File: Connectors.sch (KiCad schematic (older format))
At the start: 14 parts, among them J2 Conn_01x08_Male, J3 Conn_01x08_Male, J4 Conn_01x08_Male

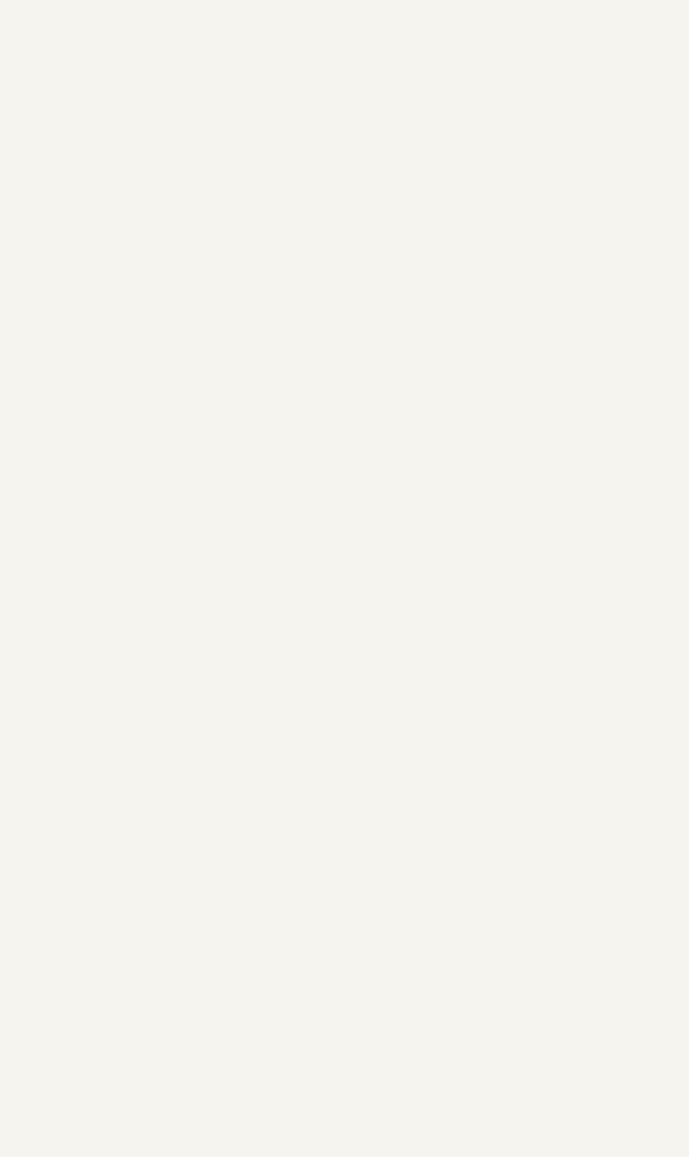
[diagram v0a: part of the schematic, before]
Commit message: start adding usb-c
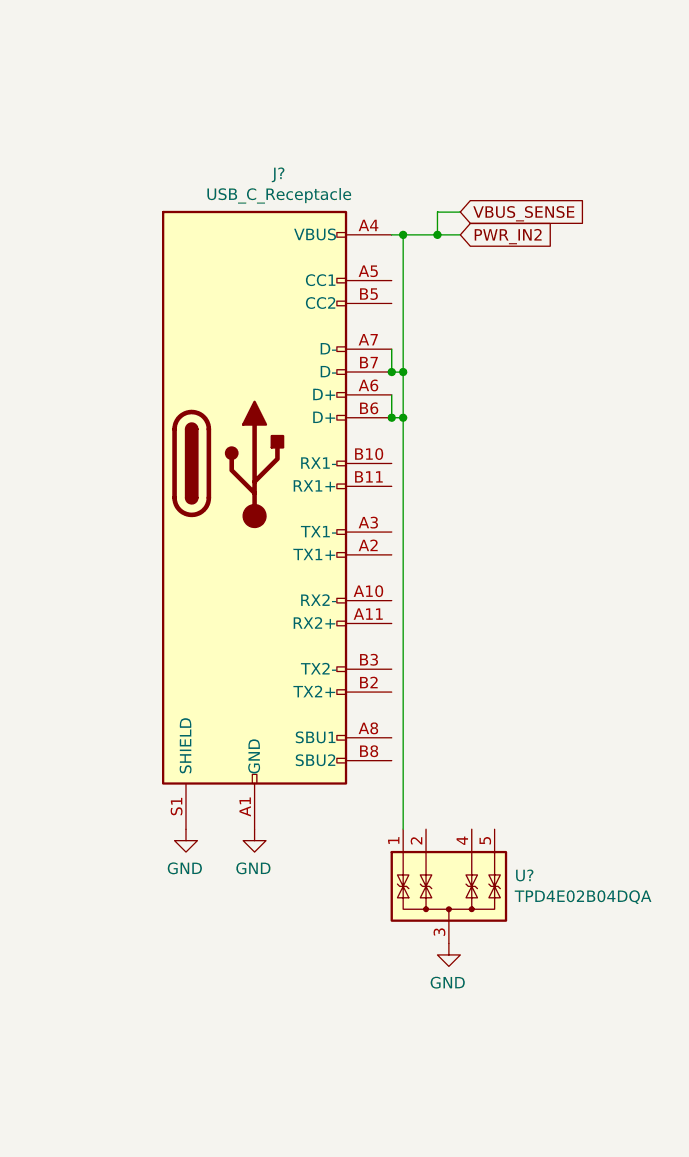
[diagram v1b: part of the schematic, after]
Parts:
- added J?: USB_C_Receptacle, symbol Connector:USB_C_Receptacle
- added U?: TPD4E02B04DQA, Package_SON:USON-10_2.5x1.0mm_P0.5mm, symbol Power_Protection:TPD4E02B04DQA
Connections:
- net GND: now also J?.A1 (GND), J?.A12 (GND), J?.B1 (GND), J?.B12 (GND), J?.S1 (SHIELD), U?.3 (G), U?.8 (G)
- new net PWR_IN2: J?.A4 (VBUS), J?.A6 (D+), J?.A7 (D-), J?.A9 (VBUS), J?.B4 (VBUS), J?.B6 (D+), J?.B7 (D-), J?.B9 (VBUS), U?.1 (IO1)
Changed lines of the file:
@@
 EndData
 $EndBitmap
+$Comp
+L Connector:USB_C_Receptacle J?
+U 1 1 61CDAA86
+P 11850 2450
+F 0 "J?" H 11957 3717 50  0000 C CNN
+F 1 "USB_C_Receptacle" H 11957 3626 50  0000 C CNN
+F 2 "" H 12000 2450 50  0001 C CNN
+F 3 "https://www.usb.org/sites/default/files/documents/usb_type-c.zip" H 12000 2450 50  0001 C CNN
+	1    11850 2450
+	1    0    0    -1
+$EndComp
+Text GLabel 12750 1350 2    50   Input ~ 0
+VBUS_SENSE
+$Comp
+L Power_Protection:TPD4E02B04DQA U?
+U 1 1 61CDF2A4
+P 12700 4350
+F 0 "U?" H 12988 4446 50  0000 L CNN
+F 1 "TPD4E02B04DQA" H 12988 4355 50  0000 L CNN
+F 2 "Package_SON:USON-10_2.5x1.0mm_P0.5mm" H 13000 4350 50  0001 L CNN
+F 3 "http://www.ti.com/lit/ds/symlink/tpd4e02b04.pdf" H 12825 4675 50  0001 C CNN
+	1    12700 4350
+	1    0    0    -1
+$EndComp
+$Comp
+L power:GND #PWR?
+U 1 1 61CE1733
+P 12700 4550
+AR Path="/61C29261/61CE1733" Ref="#PWR?"  Part="1"
+AR Path="/61E12439/61CE1733" Ref="#PWR?"  Part="1"
+F 0 "#PWR?" H 12700 4300 50  0001 C CNN
+F 1 "GND" H 12705 4377 50  0000 C CNN
+F 2 "" H 12700 4550 50  0001 C CNN
+F 3 "" H 12700 4550 50  0001 C CNN
+	1    12700 4550
+	-1   0    0    -1
+$EndComp
+$Comp
+L power:GND #PWR?
+U 1 1 61CE227D
+P 11850 4050
+AR Path="/61C29261/61CE227D" Ref="#PWR?"  Part="1"
+AR Path="/61E12439/61CE227D" Ref="#PWR?"  Part="1"
+F 0 "#PWR?" H 11850 3800 50  0001 C CNN
+F 1 "GND" H 11855 3877 50  0000 C CNN
+F 2 "" H 11850 4050 50  0001 C CNN
+F 3 "" H 11850 4050 50  0001 C CNN
+	1    11850 4050
+	-1   0    0    -1
+$EndComp
+$Comp
+L power:GND #PWR?
+U 1 1 61CE293D
+P 11550 4050
+AR Path="/61C29261/61CE293D" Ref="#PWR?"  Part="1"
+AR Path="/61E12439/61CE293D" Ref="#PWR?"  Part="1"
+F 0 "#PWR?" H 11550 3800 50  0001 C CNN
+F 1 "GND" H 11555 3877 50  0000 C CNN
+F 2 "" H 11550 4050 50  0001 C CNN
+F 3 "" H 11550 4050 50  0001 C CNN
+	1    11550 4050
+	-1   0    0    -1
+$EndComp
+Wire Wire Line
+	12450 1450 12500 1450
+Wire Wire Line
+	12500 1450 12500 2050
+Connection ~ 12500 1450
+Wire Wire Line
+	12500 1450 12650 1450
+Wire Wire Line
+	12450 2150 12450 2250
+Wire Wire Line
+	12450 1950 12450 2050
+Wire Wire Line
+	12450 2050 12500 2050
+Connection ~ 12450 2050
+Connection ~ 12500 2050
+Wire Wire Line
+	12500 2050 12500 2250
+Wire Wire Line
+	12450 2250 12500 2250
+Connection ~ 12450 2250
+Connection ~ 12500 2250
+Wire Wire Line
+	12500 2250 12500 4050
+Text GLabel 12750 1450 2    50   Input ~ 0
+PWR_IN2
+Wire Wire Line
+	12750 1350 12650 1350
+Wire Wire Line
+	12650 1350 12650 1450
+Connection ~ 12650 1450
+Wire Wire Line
+	12650 1450 12750 1450
 $EndSCHEMATC

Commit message: working
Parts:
- J6: renamed from J?; footprint (none) -> Connector_USB:USB_C_Receptacle_XKB_U262-16XN-4BVC11
- gave numbers to parts that had none: 1
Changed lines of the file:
@@
 Wire Wire Line
 	3700 3100 3700 3200
-Text GLabel 4500 2500 2    50   Input ~ 0
-STM_CH1
 Wire Wire Line
 	4500 2500 4400 2500
@@
 $EndBitmap
 $Comp
-L Connector:USB_C_Receptacle J?
+L Connector:USB_C_Receptacle J6
 U 1 1 61CDAA86
 P 11850 2450
-F 0 "J?" H 11957 3717 50  0000 C CNN
+F 0 "J6" H 11957 3717 50  0000 C CNN
 F 1 "USB_C_Receptacle" H 11957 3626 50  0000 C CNN
-F 2 "" H 12000 2450 50  0001 C CNN
+F 2 "Connector_USB:USB_C_Receptacle_XKB_U262-16XN-4BVC11" H 12000 2450 50  0001 C CNN
 F 3 "https://www.usb.org/sites/default/files/documents/usb_type-c.zip" H 12000 2450 50  0001 C CNN
 	1    11850 2450
@@
 VBUS_SENSE
 $Comp
-L Power_Protection:TPD4E02B04DQA U?
+L Power_Protection:TPD4E02B04DQA U15
 U 1 1 61CDF2A4
 P 12700 4350
-F 0 "U?" H 12988 4446 50  0000 L CNN
+F 0 "U15" H 12988 4446 50  0000 L CNN
 F 1 "TPD4E02B04DQA" H 12988 4355 50  0000 L CNN
 F 2 "Package_SON:USON-10_2.5x1.0mm_P0.5mm" H 13000 4350 50  0001 L CNN
@@
 $EndComp
 $Comp
-L power:GND #PWR?
+L power:GND #PWR0153
 U 1 1 61CE1733
 P 12700 4550
-AR Path="/61C29261/61CE1733" Ref="#PWR?"  Part="1"
+AR Path="/61C29261/61CE1733" Ref="#PWR0153"  Part="1"
 AR Path="/61E12439/61CE1733" Ref="#PWR?"  Part="1"
-F 0 "#PWR?" H 12700 4300 50  0001 C CNN
+F 0 "#PWR0153" H 12700 4300 50  0001 C CNN
 F 1 "GND" H 12705 4377 50  0000 C CNN
 F 2 "" H 12700 4550 50  0001 C CNN
@@
 $EndComp
 $Comp
-L power:GND #PWR?
+L power:GND #PWR0154
 U 1 1 61CE227D
 P 11850 4050
-AR Path="/61C29261/61CE227D" Ref="#PWR?"  Part="1"
+AR Path="/61C29261/61CE227D" Ref="#PWR0154"  Part="1"
 AR Path="/61E12439/61CE227D" Ref="#PWR?"  Part="1"
-F 0 "#PWR?" H 11850 3800 50  0001 C CNN
+F 0 "#PWR0154" H 11850 3800 50  0001 C CNN
 F 1 "GND" H 11855 3877 50  0000 C CNN
 F 2 "" H 11850 4050 50  0001 C CNN
@@
 $EndComp
 $Comp
-L power:GND #PWR?
+L power:GND #PWR0155
 U 1 1 61CE293D
 P 11550 4050
-AR Path="/61C29261/61CE293D" Ref="#PWR?"  Part="1"
+AR Path="/61C29261/61CE293D" Ref="#PWR0155"  Part="1"
 AR Path="/61E12439/61CE293D" Ref="#PWR?"  Part="1"
-F 0 "#PWR?" H 11550 3800 50  0001 C CNN
+F 0 "#PWR0155" H 11550 3800 50  0001 C CNN
 F 1 "GND" H 11555 3877 50  0000 C CNN
 F 2 "" H 11550 4050 50  0001 C CNN
@@
 Wire Wire Line
 	12650 1450 12750 1450
+Text GLabel 4500 2500 2    50   Input ~ 0
+STM_CH1
 $EndSCHEMATC

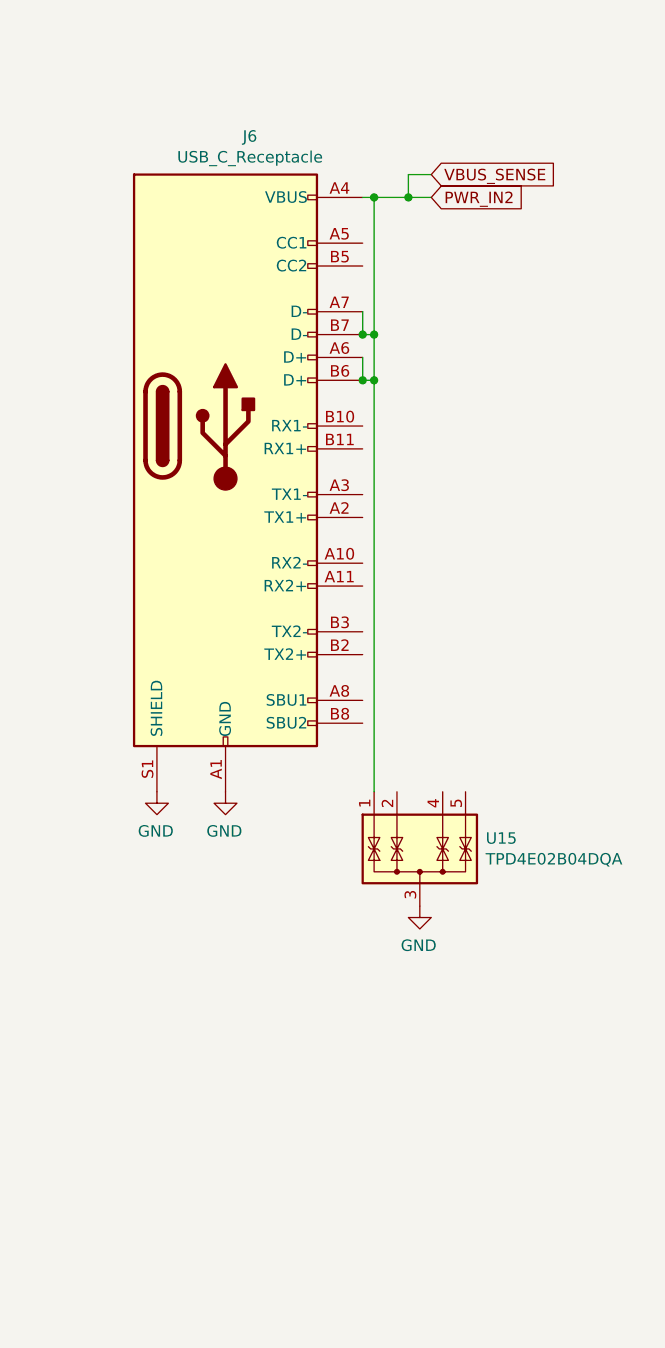
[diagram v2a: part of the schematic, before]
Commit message: start migrating to kicad v6
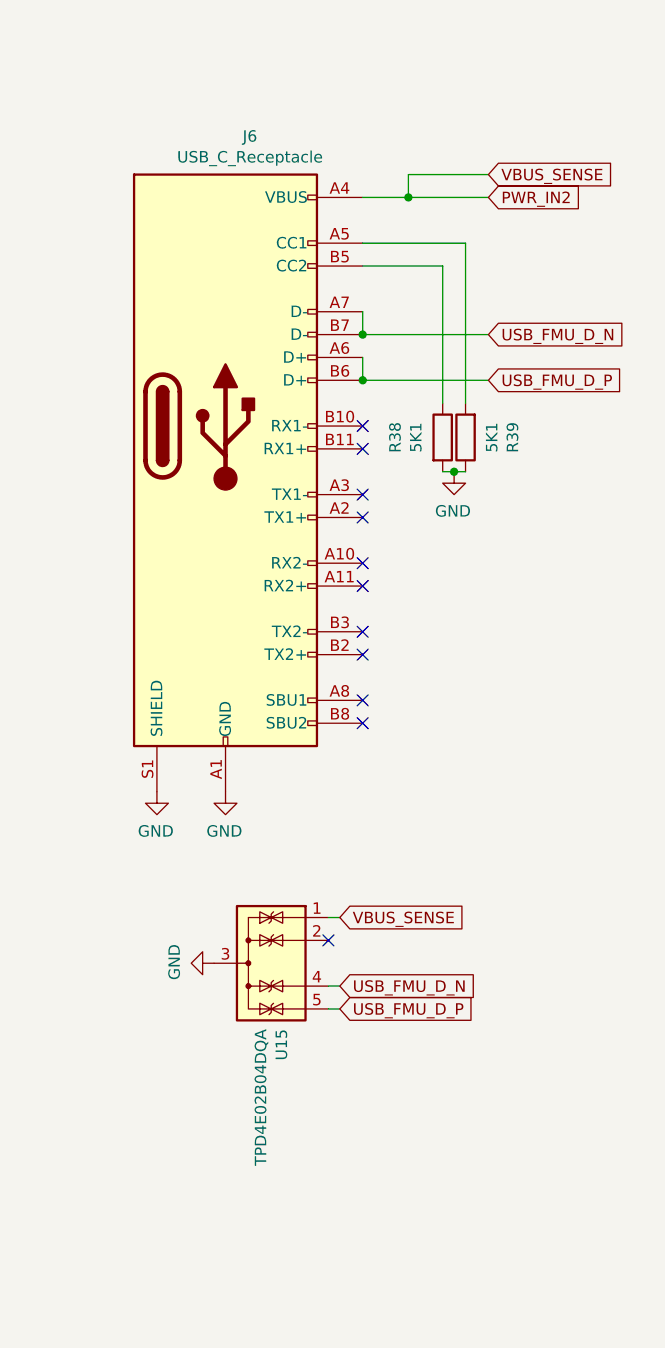
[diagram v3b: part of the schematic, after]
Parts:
- added R38, R39: 5K1, Resistor_SMD:R_0402_1005Metric, symbol Device:R
- J6: Datasheet (none) -> https://www.usb.org/sites/default/files/documents/usb_type-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; Footprint (none) -> Connector_USB:USB_C_Receptacle_XKB_U262-16XN-4BVC11; Manufacturer_Part_Number (none) -> U262-161N-4BVC11; Reference (none) -> J6; Value (none) -> USB_C_Receptacle
- U15: Datasheet (none) -> http://www.ti.com/lit/ds/symlink/tpd4e02b04.pdf; Footprint (none) -> Package_SON:USON-10_2.5x1.0mm_P0.5mm; Manufacturer_Part_Number (none) -> TPD4E02B04DQA; Reference (none) -> U15; Value (none) -> TPD4E02B04DQA
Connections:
- net GND: now also R38.2, R39.1
- net PWR_IN2: no longer J6.A6 (D+), J6.A7 (D-), J6.B6 (D+), J6.B7 (D-)
- net at J6.A5 (CC1): now also R39.2
- net at J6.B5 (CC2): now also R38.1
- net USB_FMU_D_N: now reaches U15.4 (IO3)
- net USB_FMU_D_N: now also J6.A7 (D-), J6.B7 (D-)
- net USB_FMU_D_P: now reaches U15.5 (IO4)
- net USB_FMU_D_P: now also J6.A6 (D+), J6.B6 (D+)
- no-connect marks 6 -> 17
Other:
- moved on the sheet: U15
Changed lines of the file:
@@
 EndData
 $EndBitmap
-$Comp
-L Connector:USB_C_Receptacle J6
-U 1 1 61CDAA86
-P 11850 2450
-F 0 "J6" H 11957 3717 50  0000 C CNN
-F 1 "USB_C_Receptacle" H 11957 3626 50  0000 C CNN
-F 2 "Connector_USB:USB_C_Receptacle_XKB_U262-16XN-4BVC11" H 12000 2450 50  0001 C CNN
-F 3 "https://www.usb.org/sites/default/files/documents/usb_type-c.zip" H 12000 2450 50  0001 C CNN
-	1    11850 2450
-	1    0    0    -1
-$EndComp
-Text GLabel 12750 1350 2    50   Input ~ 0
+Text GLabel 13000 1350 2    50   Input ~ 0
 VBUS_SENSE
-$Comp
-L Power_Protection:TPD4E02B04DQA U15
-U 1 1 61CDF2A4
-P 12700 4350
-F 0 "U15" H 12988 4446 50  0000 L CNN
-F 1 "TPD4E02B04DQA" H 12988 4355 50  0000 L CNN
-F 2 "Package_SON:USON-10_2.5x1.0mm_P0.5mm" H 13000 4350 50  0001 L CNN
-F 3 "http://www.ti.com/lit/ds/symlink/tpd4e02b04.pdf" H 12825 4675 50  0001 C CNN
-	1    12700 4350
-	1    0    0    -1
-$EndComp
-$Comp
-L power:GND #PWR0153
-U 1 1 61CE1733
-P 12700 4550
-AR Path="/61C29261/61CE1733" Ref="#PWR0153"  Part="1"
-AR Path="/61E12439/61CE1733" Ref="#PWR?"  Part="1"
-F 0 "#PWR0153" H 12700 4300 50  0001 C CNN
-F 1 "GND" H 12705 4377 50  0000 C CNN
-F 2 "" H 12700 4550 50  0001 C CNN
-F 3 "" H 12700 4550 50  0001 C CNN
-	1    12700 4550
-	-1   0    0    -1
-$EndComp
 $Comp
 L power:GND #PWR0154
@@
 	-1   0    0    -1
 $EndComp
-Wire Wire Line
-	12450 1450 12500 1450
-Wire Wire Line
-	12500 1450 12500 2050
-Connection ~ 12500 1450
-Wire Wire Line
-	12500 1450 12650 1450
-Wire Wire Line
-	12450 2150 12450 2250
-Wire Wire Line
-	12450 1950 12450 2050
-Wire Wire Line
-	12450 2050 12500 2050
-Connection ~ 12450 2050
-Connection ~ 12500 2050
-Wire Wire Line
-	12500 2050 12500 2250
-Wire Wire Line
-	12450 2250 12500 2250
-Connection ~ 12450 2250
-Connection ~ 12500 2250
-Wire Wire Line
-	12500 2250 12500 4050
-Text GLabel 12750 1450 2    50   Input ~ 0
+Text GLabel 13000 1450 2    50   Input ~ 0
 PWR_IN2
 Wire Wire Line
-	12750 1350 12650 1350
+	13000 1350 12650 1350
 Wire Wire Line
 	12650 1350 12650 1450
 Connection ~ 12650 1450
 Wire Wire Line
-	12650 1450 12750 1450
+	12650 1450 13000 1450
 Text GLabel 4500 2500 2    50   Input ~ 0
 STM_CH1
+Wire Wire Line
+	12450 1950 12450 2050
+Wire Wire Line
+	12450 2150 12450 2250
+Text GLabel 13000 2050 2    50   Input ~ 0
+USB_FMU_D_N
+Text GLabel 13000 2250 2    50   Input ~ 0
+USB_FMU_D_P
+Wire Wire Line
+	12450 2250 13000 2250
+Wire Wire Line
+	12450 2050 13000 2050
+Wire Wire Line
+	12450 1450 12650 1450
+Connection ~ 12450 2250
+Connection ~ 12450 2050
+$Comp
+L power:GND #PWR0153
+U 1 1 61CE1733
+P 11800 4800
+AR Path="/61C29261/61CE1733" Ref="#PWR0153"  Part="1"
+AR Path="/61E12439/61CE1733" Ref="#PWR?"  Part="1"
+F 0 "#PWR0153" H 11800 4550 50  0001 C CNN
+F 1 "GND" H 11805 4627 50  0000 C CNN
+F 2 "" H 11800 4800 50  0001 C CNN
+F 3 "" H 11800 4800 50  0001 C CNN
+	1    11800 4800
+	0    1    -1   0
+$EndComp
+$Comp
+L Power_Protection:TPD4E02B04DQA U15
+U 1 1 61CDF2A4
+P 12000 4800
+F 0 "U15" H 12288 4896 50  0000 L CNN
+F 1 "TPD4E02B04DQA" H 12288 4805 50  0000 L CNN
+F 2 "Package_SON:USON-10_2.5x1.0mm_P0.5mm" H 12300 4800 50  0001 L CNN
+F 3 "http://www.ti.com/lit/ds/symlink/tpd4e02b04.pdf" H 12125 5125 50  0001 C CNN
+F 4 "TPD4E02B04DQA" H 12000 4800 50  0001 C CNN "Manufacturer_Part_Number"
+F 5 "http://www.ti.com/lit/ds/symlink/tpd4e02b04.pdf" H 12000 4800 50  0001 C CNN "Datasheet"
+F 6 "Package_SON:USON-10_2.5x1.0mm_P0.5mm" H 12000 4800 50  0001 C CNN "Footprint"
+F 7 "U15" H 12000 4800 50  0001 C CNN "Reference"
+F 8 "TPD4E02B04DQA" H 12000 4800 50  0001 C CNN "Value"
+	1    12000 4800
+	0    1    1    0
+$EndComp
+$Comp
+L Connector:USB_C_Receptacle J6
+U 1 1 61CDAA86
+P 11850 2450
+F 0 "J6" H 11957 3717 50  0000 C CNN
+F 1 "USB_C_Receptacle" H 11957 3626 50  0000 C CNN
+F 2 "Connector_USB:USB_C_Receptacle_XKB_U262-16XN-4BVC11" H 12000 2450 50  0001 C CNN
+F 3 "https://www.usb.org/sites/default/files/documents/usb_type-c.zip" H 12000 2450 50  0001 C CNN
+F 4 "U262-161N-4BVC11" H 11850 2450 50  0001 C CNN "Manufacturer_Part_Number"
+F 5 "https://www.usb.org/sites/default/files/documents/usb_type-c.zip" H 11850 2450 50  0001 C CNN "Datasheet"
+F 6 "Connector_USB:USB_C_Receptacle_XKB_U262-16XN-4BVC11" H 11850 2450 50  0001 C CNN "Footprint"
+F 7 "J6" H 11850 2450 50  0001 C CNN "Reference"
+F 8 "USB_C_Receptacle" H 11850 2450 50  0001 C CNN "Value"
+	1    11850 2450
+	1    0    0    -1
+$EndComp
+Text GLabel 12350 4600 2    50   Input ~ 0
+VBUS_SENSE
+Text GLabel 12350 4900 2    50   Input ~ 0
+USB_FMU_D_N
+Text GLabel 12350 5000 2    50   Input ~ 0
+USB_FMU_D_P
+Wire Wire Line
+	12350 4600 12300 4600
+Wire Wire Line
+	12300 4900 12350 4900
+Wire Wire Line
+	12350 5000 12300 5000
+$Comp
+L Device:R R?
+U 1 1 6391FDB2
+P 12800 2500
+AR Path="/61B917F2/6391FDB2" Ref="R?"  Part="1"
+AR Path="/61B8EE7D/6391FDB2" Ref="R?"  Part="1"
+AR Path="/623216E9/6391FDB2" Ref="R?"  Part="1"
+AR Path="/61C29261/6391FDB2" Ref="R38"  Part="1"
+F 0 "R38" V 12593 2500 50  0000 C CNN
+F 1 "5K1" V 12684 2500 50  0000 C CNN
+F 2 "Resistor_SMD:R_0402_1005Metric" V 12730 2500 50  0001 C CNN
+F 3 "~" H 12800 2500 50  0001 C CNN
+F 4 "~" H 12800 2500 50  0001 C CNN "Datasheet"
+F 5 "Resistor_SMD:R_0402_1005Metric" H 12800 2500 50  0001 C CNN "Footprint"
+F 6 "5K1" H 12800 2500 50  0001 C CNN "Value"
+F 7 "R38" H 12800 2500 50  0001 C CNN "Reference"
+	1    12800 2500
+	1    0    0    -1
+$EndComp
+$Comp
+L power:GND #PWR0144
+U 1 1 639482DC
+P 12850 2650
+AR Path="/61C29261/639482DC" Ref="#PWR0144"  Part="1"
+AR Path="/61E12439/639482DC" Ref="#PWR?"  Part="1"
+F 0 "#PWR0144" H 12850 2400 50  0001 C CNN
+F 1 "GND" H 12855 2477 50  0000 C CNN
+F 2 "" H 12850 2650 50  0001 C CNN
+F 3 "" H 12850 2650 50  0001 C CNN
+	1    12850 2650
+	-1   0    0    -1
+$EndComp
+Connection ~ 12850 2650
+Wire Wire Line
+	12850 2650 12800 2650
+Wire Wire Line
+	12900 2650 12850 2650
+$Comp
+L Device:R R?
+U 1 1 6392B246
+P 12900 2500
+AR Path="/61B917F2/6392B246" Ref="R?"  Part="1"
+AR Path="/61B8EE7D/6392B246" Ref="R?"  Part="1"
+AR Path="/623216E9/6392B246" Ref="R?"  Part="1"
+AR Path="/61C29261/6392B246" Ref="R39"  Part="1"
+F 0 "R39" V 12693 2500 50  0000 C CNN
+F 1 "5K1" V 12784 2500 50  0000 C CNN
+F 2 "Resistor_SMD:R_0402_1005Metric" V 12830 2500 50  0001 C CNN
+F 3 "~" H 12900 2500 50  0001 C CNN
+F 4 "~" H 12900 2500 50  0001 C CNN "Datasheet"
+F 5 "Resistor_SMD:R_0402_1005Metric" H 12900 2500 50  0001 C CNN "Footprint"
+F 6 "5K1" H 12900 2500 50  0001 C CNN "Value"
+F 7 "R39" H 12900 2500 50  0001 C CNN "Reference"
+	1    12900 2500
+	-1   0    0    1
+$EndComp
+Wire Wire Line
+	12800 2350 12800 1750
+Wire Wire Line
+	12800 1750 12450 1750
+Wire Wire Line
+	12900 2350 12900 1650
+Wire Wire Line
+	12900 1650 12450 1650
+NoConn ~ 12450 3650
+NoConn ~ 12450 3750
+NoConn ~ 12450 3450
+NoConn ~ 12450 3350
+NoConn ~ 12450 3150
+NoConn ~ 12450 3050
+NoConn ~ 12450 2850
+NoConn ~ 12450 2750
+NoConn ~ 12450 2550
+NoConn ~ 12450 2450
+NoConn ~ 12300 4700
 $EndSCHEMATC
